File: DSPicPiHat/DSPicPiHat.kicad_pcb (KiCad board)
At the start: 2 copper layers, 65 x 66.5 mm, 91 parts, among them J1 Conn_01x09_Female, J2 Conn_01x04_Female, J4 Conn_PIC_ICSP_ICD, J5 USB_C_Receptacle_USB2.0, J6 PowerInput, J8 RasPiHeaders, SW1 POWER_Select, SW2 SW_DIP_x08, U1 DSPIC33CH512MP508T-I_PT, U10 DF5A6.2CJE_LM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

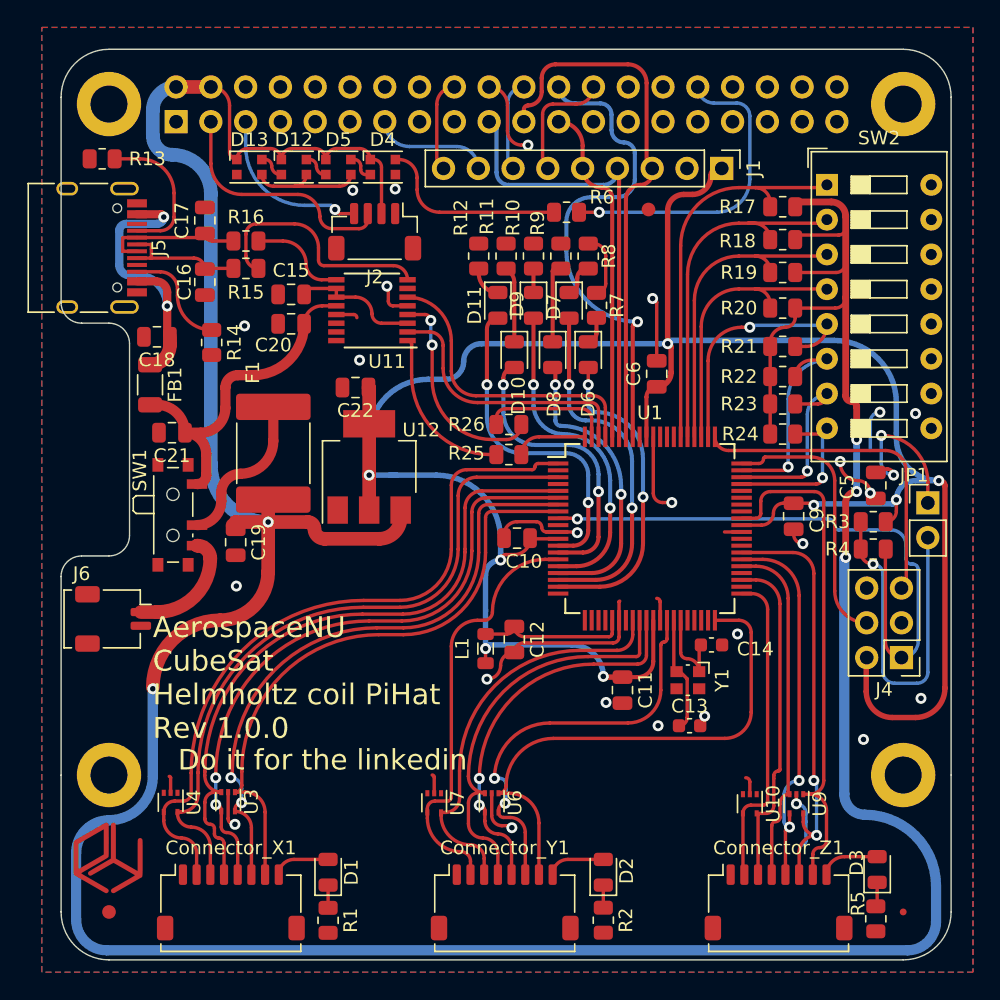
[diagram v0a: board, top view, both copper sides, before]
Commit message: filling in unkown values and footprints
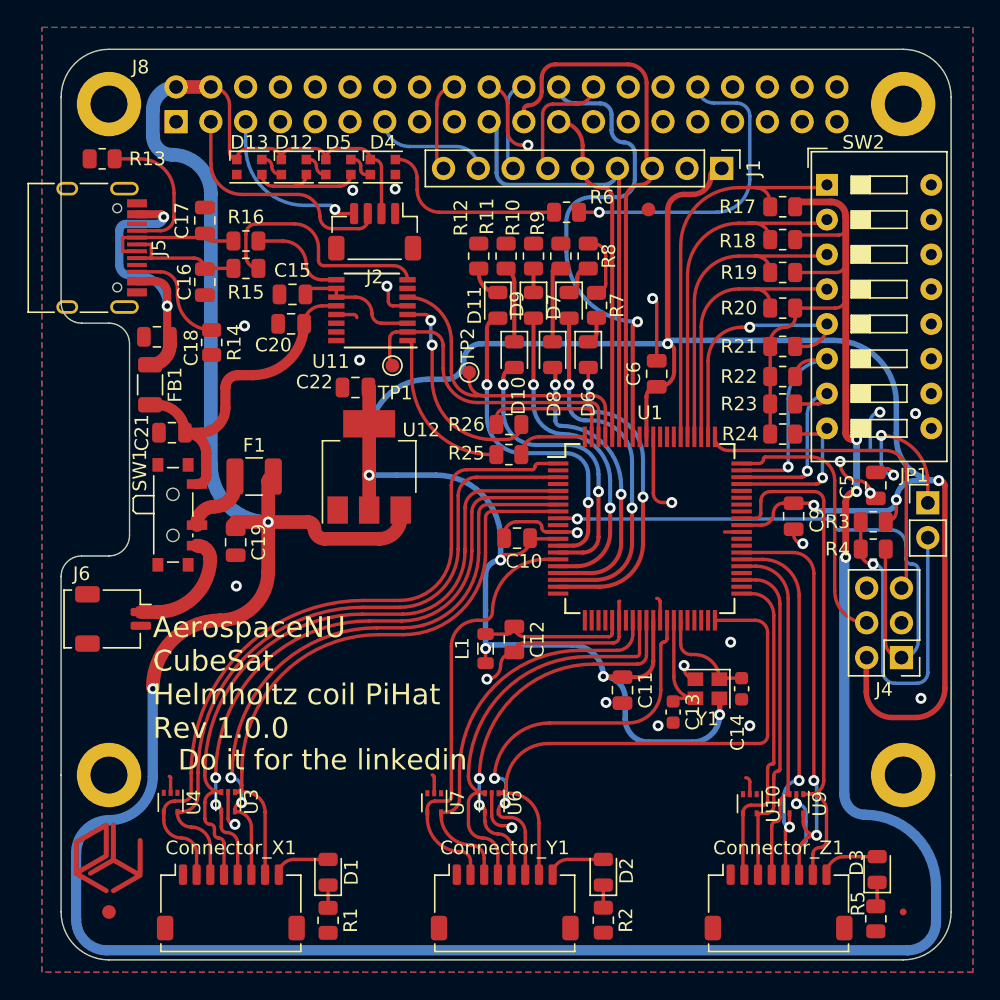
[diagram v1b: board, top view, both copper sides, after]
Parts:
- added TP1: TestPoint, TestPoint:TestPoint_Pad_D1.0mm, F.Cu at (80.7, 96.6)
- added TP2: TestPoint, TestPoint:TestPoint_Pad_D1.0mm, F.Cu at (86.3, 97.1)
- C5: value find val -> .1 uf
- D10, D11, D6, D7, D8, D9: value LED -> Blue_Led
- F1: value 3.5 A(?) -> 5 a; footprint Fuse:Fuse_2920_7451Metric -> Fuse:Fuse_1210_3225Metric
- R10, R11, R12, R7, R8, R9: value R_Small -> 0 o
- Y1: value 16MHz -> 100MHz; footprint Crystal:Crystal_SMD_Abracon_ABM10-4Pin_2.5x2.0mm -> Crystal:Crystal_SMD_2520-4Pin_2.5x2.0mm
- moved G*** 7.39 mm to (99.1, 104.0)
- moved C14 3.88 mm to (106.2, 120.2), turned to -90 degrees
- moved F1 2.20 mm to (70.6, 104.7), turned to 0 degrees
- moved C13 1.56 mm to (101.2, 121.9), turned to -90 degrees
- moved Y1 1.56 mm to (103.7, 120.2), turned to 180 degrees
- moved C15 0.10 mm to (73.4, 91.4)
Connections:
- Y1 pad 2: OSCI -> AVSS
- Y1 pad 3: (no net) -> OSCI
- Y1 pad 4: (no net) -> VDD
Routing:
- net VDD: track 176.2 -> 190.1 mm, vias 8 -> 9
- net Net-(F1-Pad1): track 11.6 -> 5.02 mm
- net U1RTS: track 19.7 -> 23.3 mm
- net EXT_ADC_Y_03: track 38.4 -> 41.6 mm
- net U1CTS: track 21.9 -> 24.2 mm
- net +5V: track 263.4 -> 265.2 mm
- net AVSS: track 80.3 -> 81.8 mm
- net OSCO: track 6.48 -> 7.59 mm
- net EXT_Z_PWM_00: track 23.3 -> 23.8 mm

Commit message: removed islands, added more vias, fixed routing, added no connect.
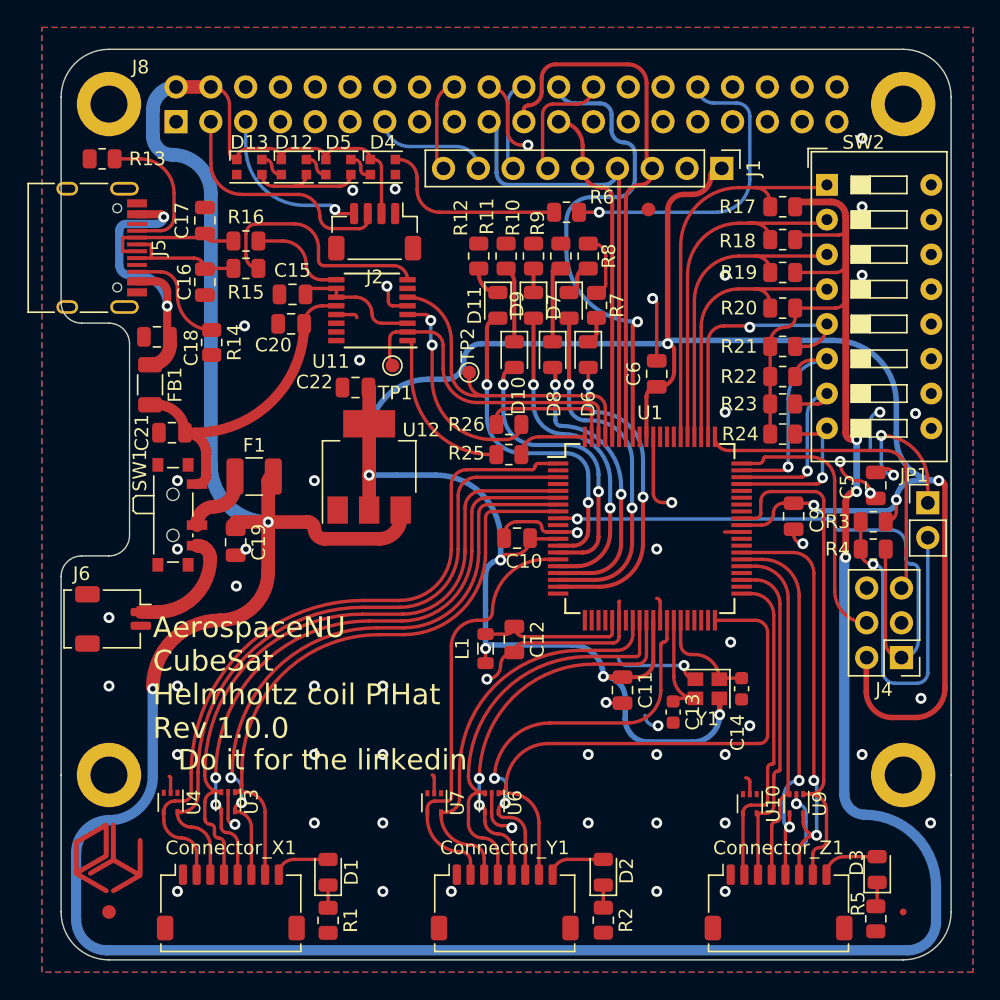
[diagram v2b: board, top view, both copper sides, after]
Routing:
- net AVSS: track 81.8 -> 89.4 mm, vias 25 -> 57
- net DIP_04: track 18.7 -> 19.5 mm
- net VBUS_USBC: track 25.2 -> 24.5 mm
- net (no net): vias 0 -> 1

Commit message: Added more vias, removed some hanging ground pours, updated drc and fixed any errors.
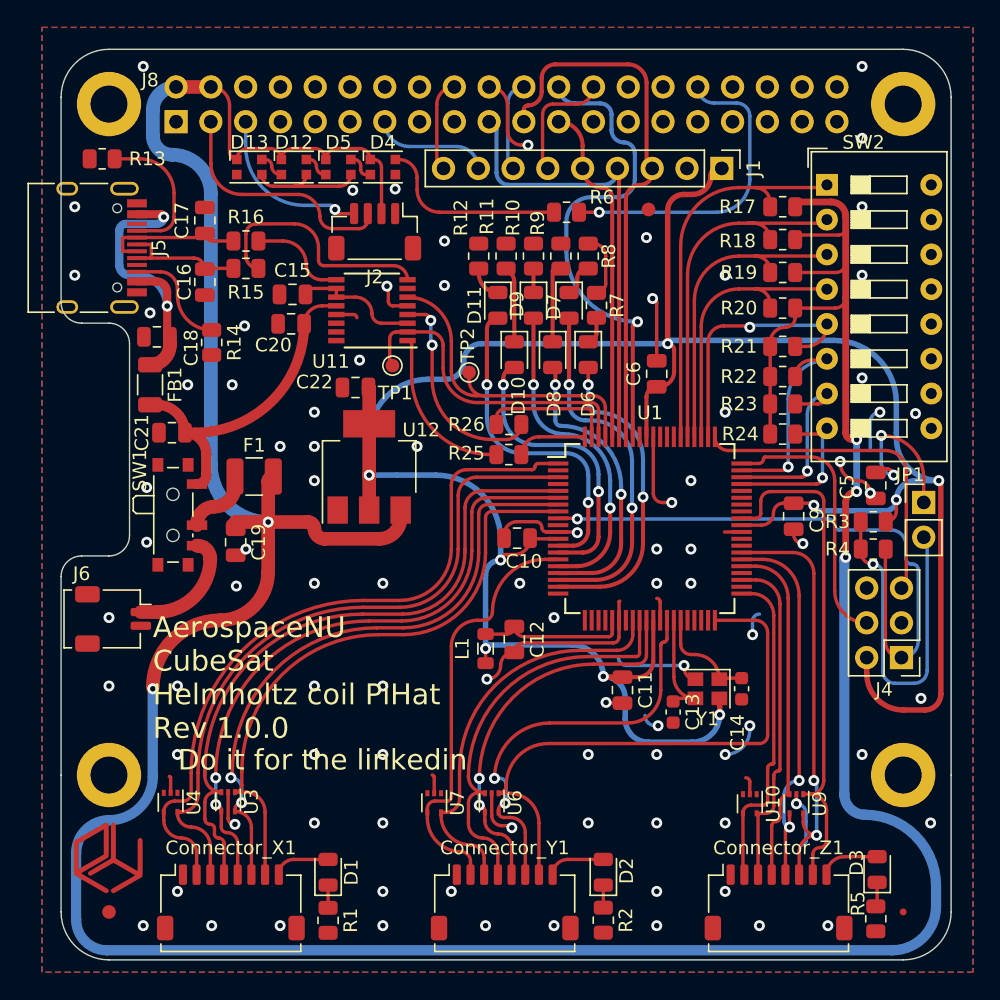
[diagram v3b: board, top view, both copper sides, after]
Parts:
- moved JP1 0.30 mm to (119.5, 106.6)
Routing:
- net AVSS: track 89.4 -> 94.3 mm, vias 57 -> 90
- net VDD: track 190.1 -> 188.6 mm
- net +5V: track 265.2 -> 264.7 mm
- net (no net): vias 1 -> 0

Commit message: made small fixes and finishing touches
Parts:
- removed REF**: Fiducial_0.5mm_Mask1.5mm, Fiducial:Fiducial_0.5mm_Mask1.5mm
- removed REF** (x2): Fiducial_1mm_Mask2mm, Fiducial:Fiducial_1mm_Mask2mm
- added FID1: Fiducial, Fiducial:Fiducial_1mm_Mask2mm, F.Cu at (118.0, 136.5)
- added FID2: Fiducial, Fiducial:Fiducial_1mm_Mask2mm, F.Cu at (60.0, 136.5)
- added FID3: Fiducial, Fiducial:Fiducial_1mm_Mask2mm, F.Cu at (99.4, 85.2)
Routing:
- net EXT_ADC_Z_01: track 27.9 -> 28.6 mm
- net AVSS: track 94.3 -> 94.9 mm, vias 90 -> 89
